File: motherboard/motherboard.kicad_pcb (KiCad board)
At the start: 2 copper layers, 85 x 56.5 mm, 34 parts, among them J1 Conn_01x02_Male, J2 Conn_01x02_Male, J3 Conn_01x02_Male, J4 Conn_01x02_Male, J5 Conn_01x02_Male, J6 XLR3, J7 Conn_01x02_Male, P1 Raspberry_Pi_+_Conn, Q1 Q_NMOS_GSD, Q2 Q_NMOS_GSD, U1 74AUC2G04, U2 4081, U3 TLC272

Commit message: Rev1.0 as sent to print
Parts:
- U2: value 4081 -> quad_and
- U3: footprint Package_SO:TSSOP-8_4.4x3mm_P0.65mm -> Package_SO:SOIC-8_3.9x4.9mm_P1.27mm
- moved C1 3.90 mm to (97.3, 87.1)
- moved U1 3.13 mm to (106.9, 70.2), turned to 180 degrees
- moved U3 2.72 mm to (98.2, 76.1), turned to 180 degrees
- moved D3 0.81 mm to (70.2, 77.5), turned to 90 degrees
- moved D2 0.24 mm to (73.7, 76.8)
- moved R10 0.24 mm to (66.6, 76.8)
- moved R11 0.24 mm to (66.6, 80.1), turned to 180 degrees
- moved R9 0.24 mm to (66.6, 73.4)
- moved D1 0.11 mm to (108.3, 85.9)
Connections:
- J6 pad 1: /Temp_interface/+3.3V -> Net-(J6-Pad1)
- J6 pad 2: Net-(J6-Pad2) -> /Temp_interface/+3.3V
- R10 pad 1: Net-(J6-Pad2) -> Net-(J6-Pad1)
- R11 pad 2: Net-(J6-Pad2) -> Net-(J6-Pad1)
- U1 pad 1: /SSR_interface/SSR1_GPIO -> /SSR_interface/SSR2_GPIO
- U1 pad 3: /SSR_interface/SSR2_GPIO -> /SSR_interface/SSR1_GPIO
- U2 pad 2: /SSR_interface/SSR2_GPIO -> /SSR_interface/SSR1_GPIO
- U2 pad 3: /SSR_interface/SSR_driver_1/sig_in -> /SSR_interface/SSR_driver_2/sig_in
- U2 pad 4: /SSR_interface/SSR_driver_2/sig_in -> /SSR_interface/SSR2_GPIO
- U2 pad 5: /SSR_interface/SSR1_GPIO -> Net-(U1-Pad4)
- U2 pad 6: Net-(U1-Pad4) -> /SSR_interface/SSR_driver_1/sig_in
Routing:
- net +5V: track 0.00 -> 108.7 mm, vias 0 -> 3
- net /Temp_interface/+3.3V: track 0.00 -> 59.0 mm
- net Net-(R8-Pad1): track 0.00 -> 41.9 mm
- net /SSR_interface/SSR2_GPIO: track 6.66 -> 46.7 mm, vias 0 -> 1
- net /SSR_interface/SSR_driver_2/indicator: track 0.00 -> 39.6 mm
- net Net-(R1-Pad2): track 0.00 -> 36.3 mm
- net /SSR_interface/SSR1_GPIO: track 0.00 -> 35.2 mm, vias 0 -> 1
- net /Temp_interface/TEMP_GPIO: track 0.00 -> 33.7 mm
- net /SSR_interface/SSR_driver_1/indicator: track 0.00 -> 30.5 mm
- net Net-(R7-Pad1): track 0.00 -> 29.6 mm
- net Net-(C1-Pad1): track 0.00 -> 18.8 mm
- net /SSR_interface/SSR_driver_2/sig_in: track 0.00 -> 16.5 mm
- net /SSR_interface/SSR_driver_1/sig_in: track 0.00 -> 13.9 mm
- net Net-(J6-Pad1): track 0.00 -> 12.5 mm
- net Net-(U1-Pad6): track 0.00 -> 10.1 mm
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- added copper zone on B.Cu, net GND
- added copper zone on F.Cu, net GND
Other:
- outline, holes or cut-outs redrawn
- net class Default: via_dia 0.6 -> 0.8
- rule trace_min: 0.01 -> 0.13
- board text added: "Bryggan motherboard v1.0"

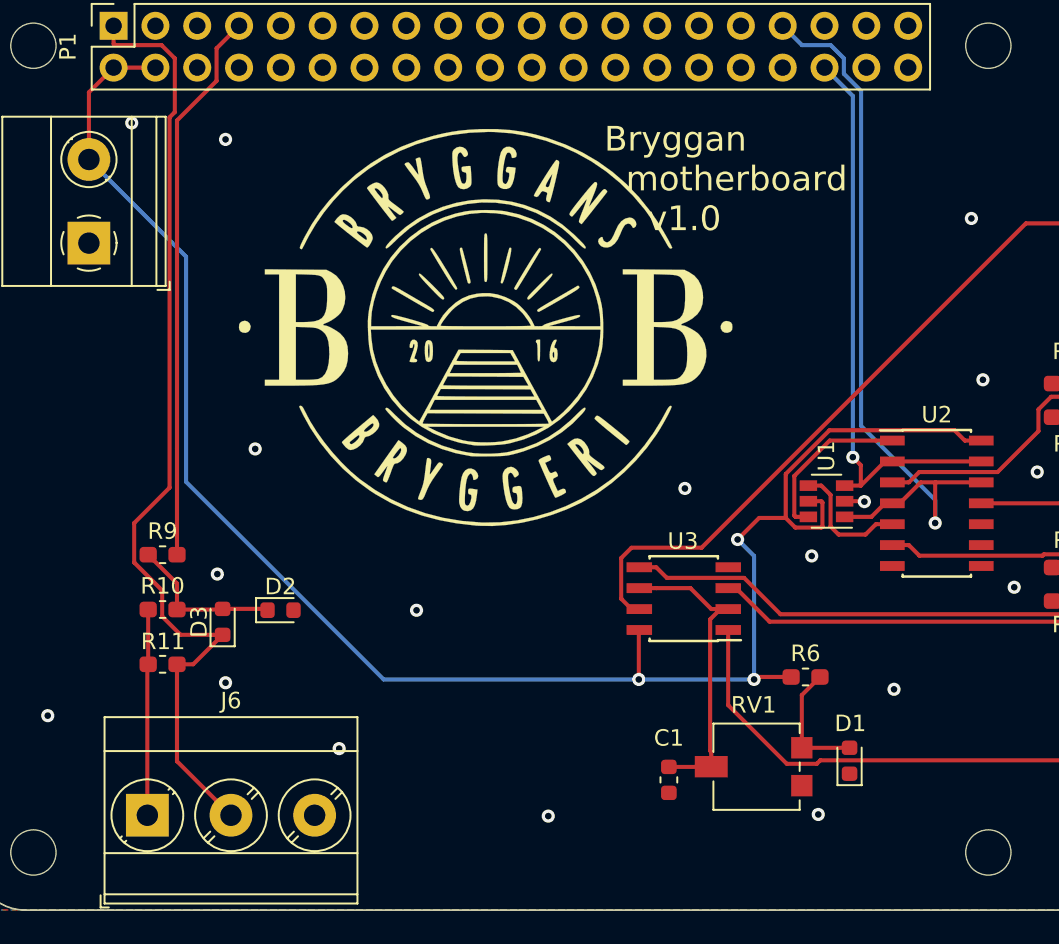
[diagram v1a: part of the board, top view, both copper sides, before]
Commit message: Added connector and hier. pins for temp
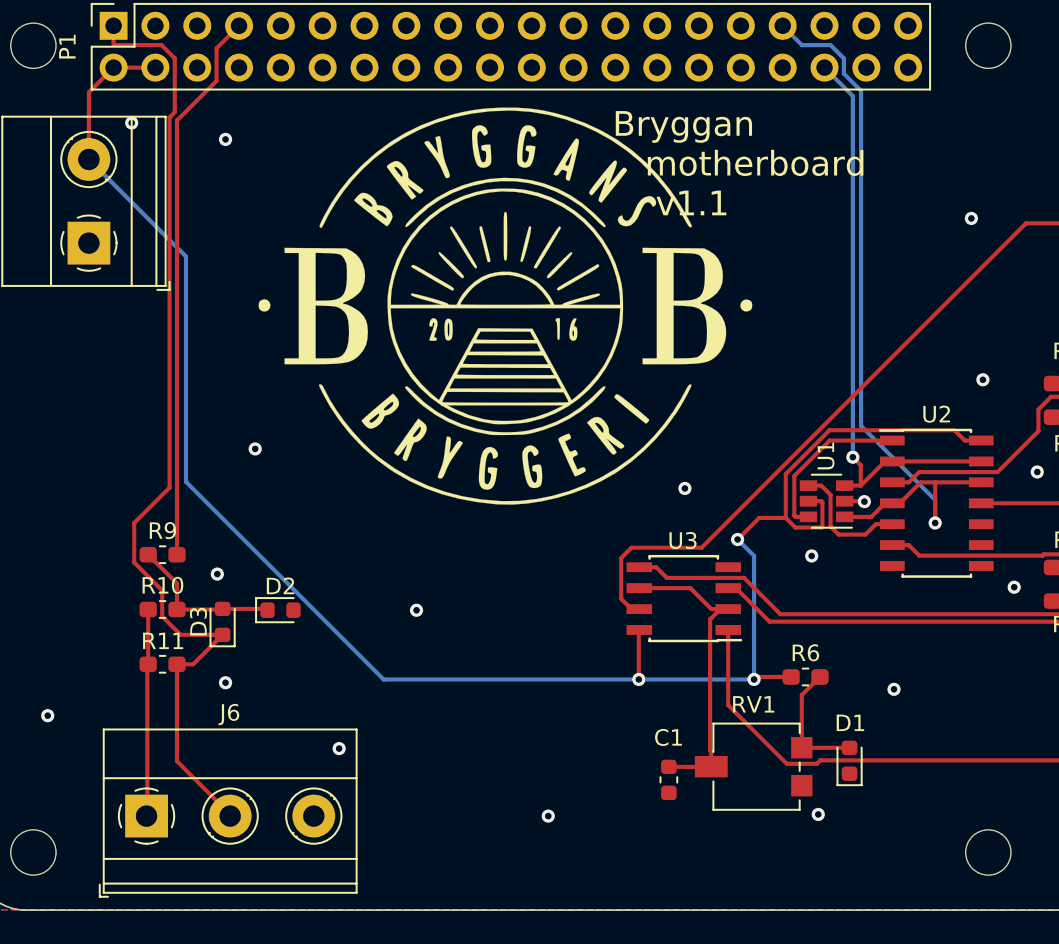
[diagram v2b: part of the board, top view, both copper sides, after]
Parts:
- J6: value XLR3 -> Conn_01x03_Male; footprint TerminalBlock_Phoenix:TerminalBlock_Phoenix_MKDS-3-3-5.08_1x03_P5.08mm_Horizontal -> TerminalBlock_Phoenix:TerminalBlock_Phoenix_MKDS-1,5-3-5.08_1x03_P5.08mm_Horizontal
- moved G*** 1.77 mm to (87.4, 58.3)
- moved J6 0.07 mm to (65.6, 89.3)
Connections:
- net /SSR_interface/SSR_driver_1/ssr_in renamed /SSR_in_1_enc
- net /SSR_interface/SSR_driver_2/ssr_in renamed /SSR_in_2_enc
- net /Temp_interface/+3.3V renamed /TEMP_IN_PWR
- net Net-(J6-Pad1) renamed /TEMP_IN_MEAS
- J1 pad 2: +5V -> /5V+
- P1 pad 2: +5V -> /5V+
- P1 pad 4: +5V -> /5V+
- U1 pad 1: /SSR_interface/SSR2_GPIO -> /SSR_interface/SSR1_GPIO
- U1 pad 3: /SSR_interface/SSR1_GPIO -> /SSR_interface/SSR2_GPIO
- U2 pad 1: Net-(U1-Pad6) -> Net-(U1-Pad4)
- U2 pad 5: Net-(U1-Pad4) -> Net-(U1-Pad6)
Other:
- board text added: "Bryggan motherboard v1.1"
- board text removed: "Bryggan motherboard v1.0"

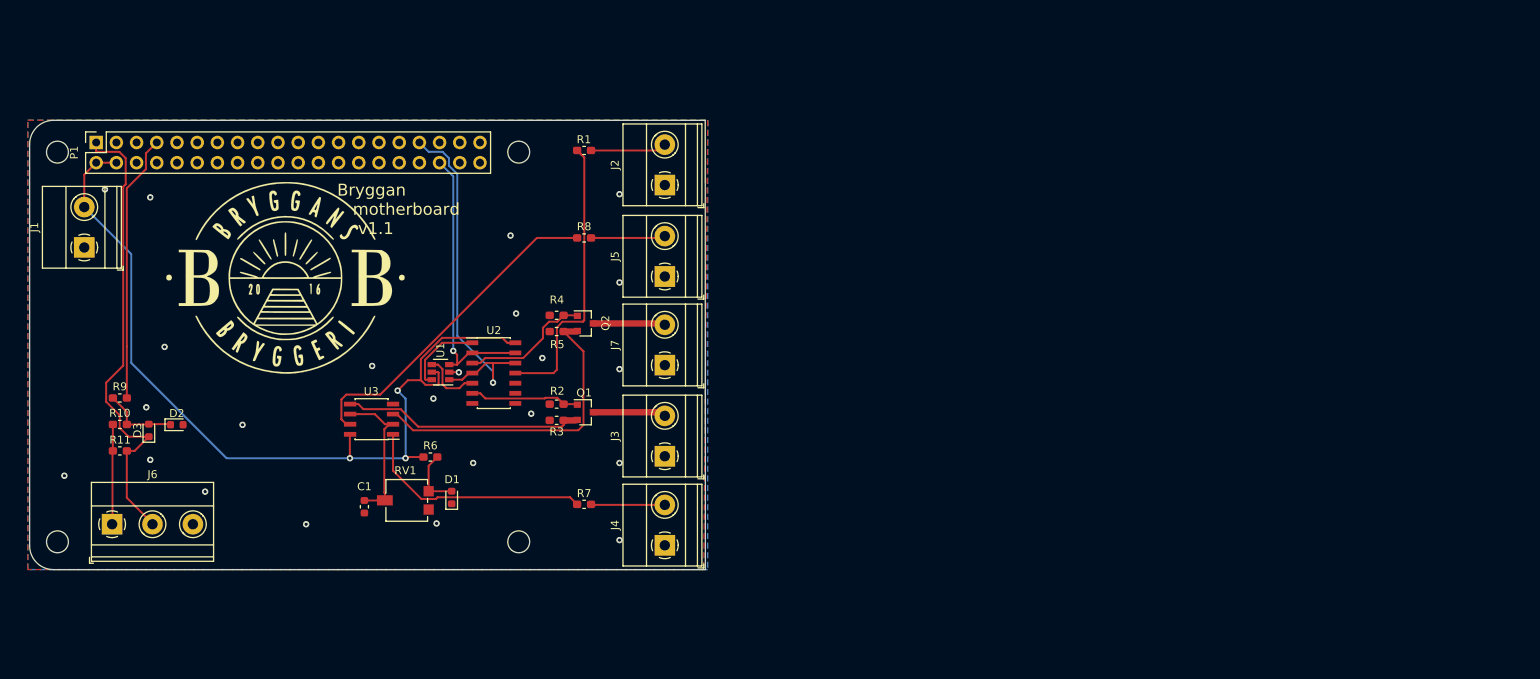
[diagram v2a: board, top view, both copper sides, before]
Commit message: WIP: Motherboard v1.1
 - Moved all connectors to root hierarchical sheet => More modular
 - Removed GND connectors for the 24VDC signals (not needed)
 - Changed 24VDC connectors to a single 1x8 phoenix connector
 - Removed connectors for SSR indicator and error signal. Indicators are
   redundant (230V lamp directly on SSR out phase instead). Error
   potentially useful. Instead these signals should be feedbacked to
   rbpi.

PCB is in shambles because of this
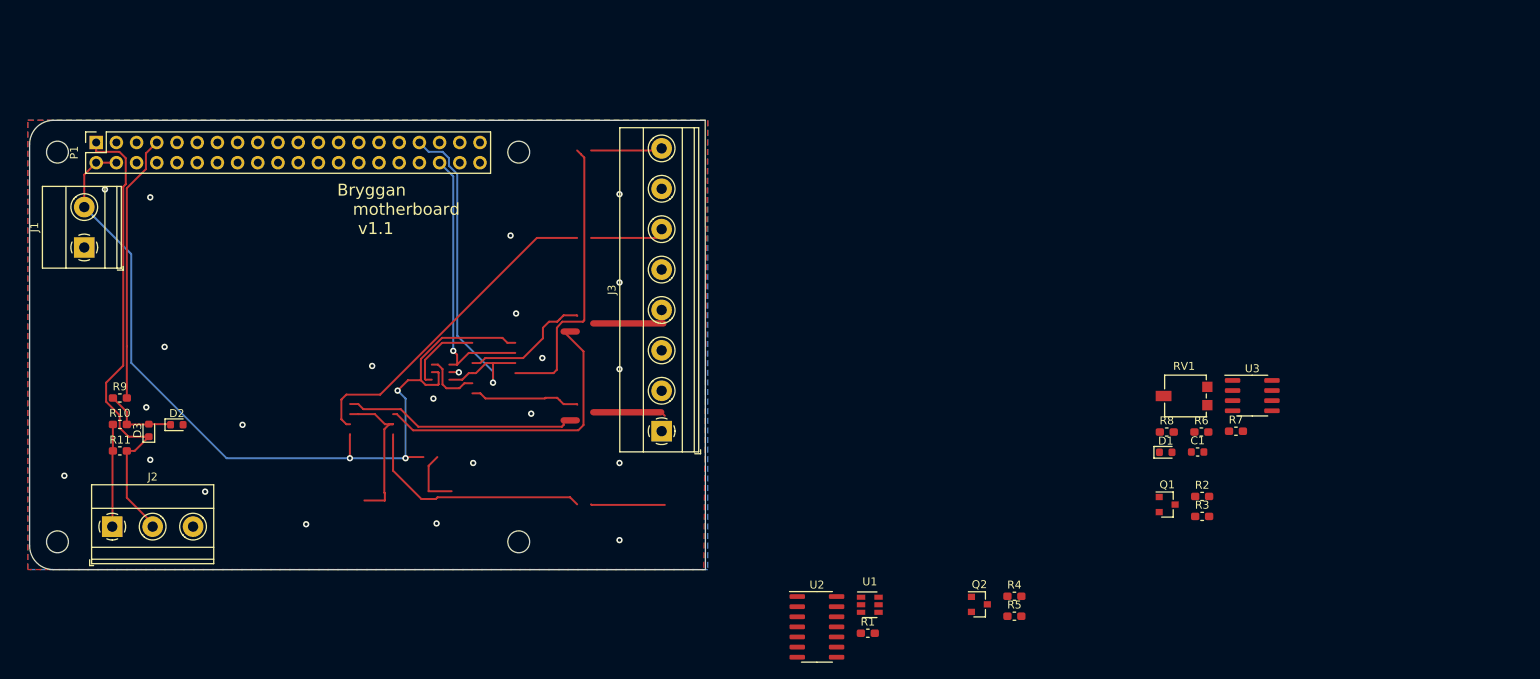
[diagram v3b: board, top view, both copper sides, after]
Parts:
- removed G***: LOGO, graphic:bryggans_logo
- removed J4, J5, J7: Conn_01x02_Male, TerminalBlock_Phoenix:TerminalBlock_Phoenix_MKDS-1,5-2-5.08_1x02_P5.08mm_Horizontal
- removed J6: Conn_01x03_Male, TerminalBlock_Phoenix:TerminalBlock_Phoenix_MKDS-1,5-3-5.08_1x03_P5.08mm_Horizontal
- J2: value Conn_01x02_Male -> Temp_connector; footprint TerminalBlock_Phoenix:TerminalBlock_Phoenix_MKDS-1,5-2-5.08_1x02_P5.08mm_Horizontal -> TerminalBlock_Phoenix:TerminalBlock_Phoenix_MKDS-1,5-3-5.08_1x03_P5.08mm_Horizontal
- J3: value Conn_01x02_Male -> 24V_connector; footprint TerminalBlock_Phoenix:TerminalBlock_Phoenix_MKDS-1,5-2-5.08_1x02_P5.08mm_Horizontal -> TerminalBlock_Phoenix:TerminalBlock_Phoenix_MKDS-1,5-8-5.08_1x08_P5.08mm_Horizontal
- moved U3 110.8 mm to (209.0, 73.1), turned to 0 degrees
- moved C1 105.0 mm to (202.1, 80.2), turned to 0 degrees
- moved RV1 98.8 mm to (200.6, 73.2)
- moved R6 97.0 mm to (202.6, 77.7)
- moved D1 90.0 mm to (198.1, 80.3), turned to 0 degrees
- moved R7 82.5 mm to (206.9, 77.6)
- moved R3 82.1 mm to (202.7, 88.3), turned to 0 degrees
- moved R2 82.0 mm to (202.7, 85.8), turned to 0 degrees
- moved J2 81.7 mm to (65.6, 89.6), turned to 0 degrees
- moved R8 77.2 mm to (198.2, 77.7)
- moved Q1 74.1 mm to (198.3, 86.8)
- moved R1 70.4 mm to (160.6, 103.0), turned to 0 degrees
- moved R5 67.8 mm to (179.1, 100.9), turned to 0 degrees
- moved R4 67.5 mm to (179.1, 98.4), turned to 0 degrees
- moved U1 61.4 mm to (160.9, 99.4), turned to 0 degrees
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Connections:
- J2 pad 1: GND -> /TEMP_IN_MEAS
- J2 pad 2: Net-(J2-Pad2) -> /TEMP_IN_PWR
- J3 pad 1: GND -> /SSR_in_1_enc
- J3 pad 2: /SSR_in_1_enc -> /SSR_in_2_enc
- R1 pad 1: Net-(J2-Pad2) -> /SSR_interface/error_signal
- R7 pad 2: Net-(J4-Pad2) -> /SSR_interface/indicator_1_pi
- R8 pad 2: Net-(J5-Pad2) -> /SSR_interface/indicator_2_pi
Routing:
- net /5V+: track 0.00 -> 108.7 mm, vias 0 -> 3
- net +5V: track 108.7 -> 0.00 mm, vias 3 -> 0
- net Net-(J3-Pad8): track 0.00 -> 9.58 mm
- net Net-(J2-Pad2): track 9.58 -> 0.00 mm
- net Net-(J5-Pad2): track 9.37 -> 0.00 mm
- net /220V_4: track 0.00 -> 9.37 mm

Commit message: WIP: Motherboard v1.1
  Cosmetic changes
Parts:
- moved U2 75.2 mm to (213.3, 55.6), turned to 180 degrees
- moved R1 66.8 mm to (206.9, 54.8)
- moved U1 61.5 mm to (206.6, 58.4), turned to 180 degrees
- moved Q2 53.3 mm to (215.8, 65.4)
- moved R4 53.3 mm to (220.2, 64.4)
- moved R5 53.3 mm to (220.2, 66.9)
- moved R2 23.0 mm to (211.1, 64.4)
- moved Q1 23.0 mm to (206.7, 65.4)
- moved R3 23.0 mm to (211.1, 66.9)
- moved R7 3.69 mm to (210.6, 77.7), turned to 180 degrees
- moved C1 0.60 mm to (202.7, 80.2)
- turned R8 to 180 degrees
- turned RV1 to 180 degrees
- turned U3 to 180 degrees
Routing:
- net Net-(R8-Pad1): track 41.9 -> 93.7 mm
- net Net-(C1-Pad1): track 18.8 -> 57.4 mm
- net /SSR_interface/SSR_driver_2/indicator: track 39.6 -> 4.75 mm
- net Net-(R7-Pad1): track 29.6 -> 2.68 mm
- net /SSR_interface/SSR_driver_1/sig_in: track 13.9 -> 39.7 mm
- net Net-(D1-Pad2): track 7.66 -> 32.7 mm
- net Net-(U1-Pad4): track 7.72 -> 22.9 mm
- net /SSR_interface/SSR_driver_2/sig_in: track 16.5 -> 31.1 mm
- net Net-(U1-Pad6): track 10.1 -> 23.6 mm
- net /SSR_interface/SSR2_GPIO: track 46.7 -> 55.5 mm
- net /SSR_interface/SSR1_GPIO: track 35.2 -> 43.7 mm
- net /SSR_interface/SSR_driver_1/indicator: track 30.5 -> 35.2 mm
- net Net-(R1-Pad2): track 36.3 -> 39.7 mm
